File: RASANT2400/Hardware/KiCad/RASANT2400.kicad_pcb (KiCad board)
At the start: 2 copper layers, 60.3 x 51.4 mm, 0 parts

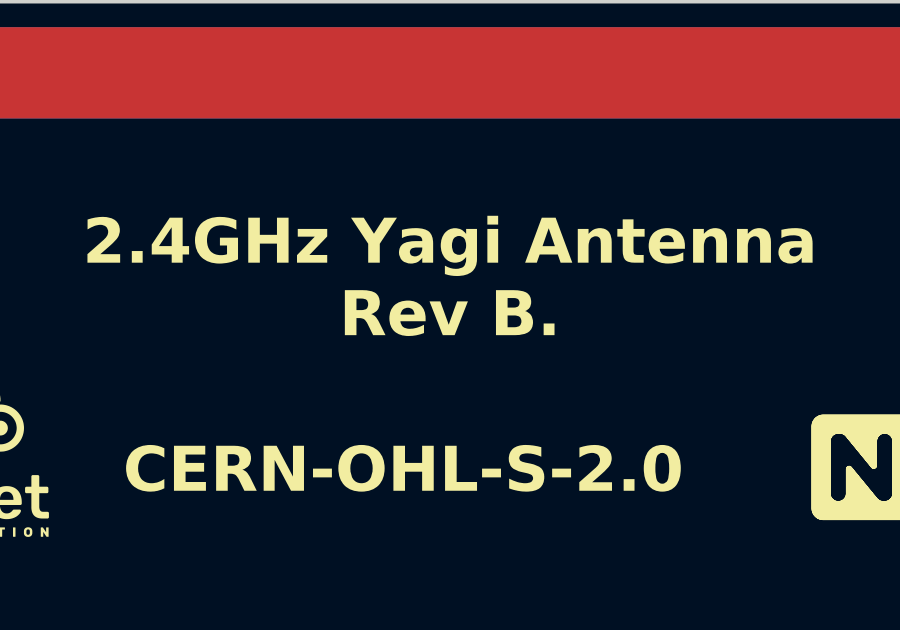
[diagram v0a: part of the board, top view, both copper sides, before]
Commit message: Udpated version Rev C with opeoinmg in the solder mask to allow soldering of SMA connectors.
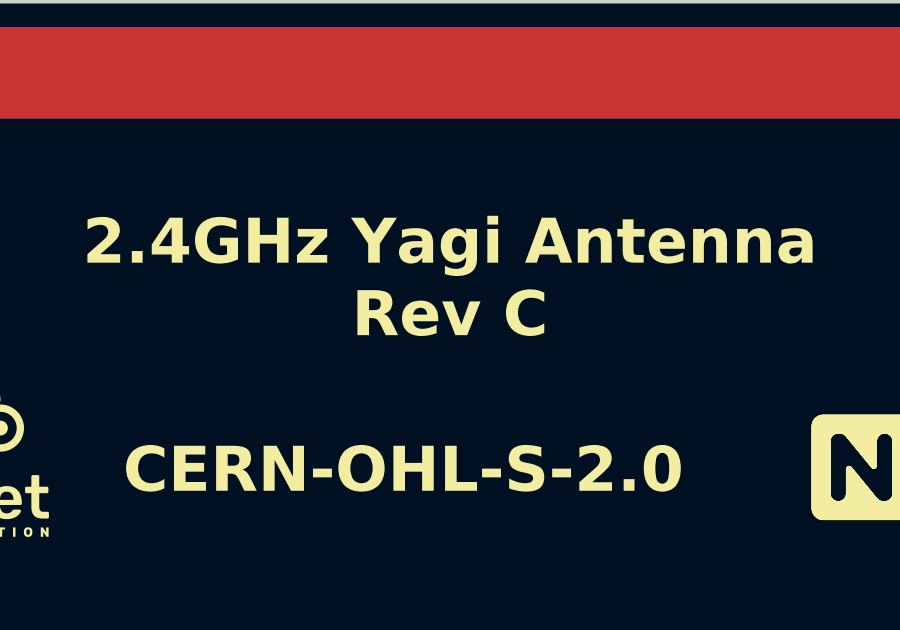
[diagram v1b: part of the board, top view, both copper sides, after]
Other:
- board text added: "2.4GHz Yagi Antenna Rev C"
- board text removed: "2.4GHz Yagi Antenna Rev B."
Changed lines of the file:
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@@
 			(outputformat 1)
 			(mirror no)
-			(drillshape 1)
+			(drillshape 0)
 			(scaleselection 1)
-			(outputdirectory "")
+			(outputdirectory "../Production/")
 		)
 	)
@@
 		(layer "F.Cu")
 	)
+	(gr_rect
+		(start 146.67 122.32)
+		(end 153.74 126.93)
+		(stroke
+			(width 0.1)
+			(type default)
+		)
+		(fill yes)
+		(layer "F.Mask")
+	)
 	(gr_poly
 		(pts
@@
 		(layer "B.Cu")
 	)
+	(gr_rect
+		(start 146.69 122.25)
+		(end 153.72 126.86)
+		(stroke
+			(width 0.1)
+			(type default)
+		)
+		(fill yes)
+		(layer "B.Mask")
+	)
 	(gr_poly
 		(pts
@@
 		)
 	)
-	(gr_text "2.4GHz Yagi Antenna\nRev B."
+	(gr_text "2.4GHz Yagi Antenna\nRev C"
 		(at 150.3 86.912533 0)
 		(layer "F.SilkS")
